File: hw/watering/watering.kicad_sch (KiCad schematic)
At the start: 5 parts, among them J2 USB_C_Receptacle

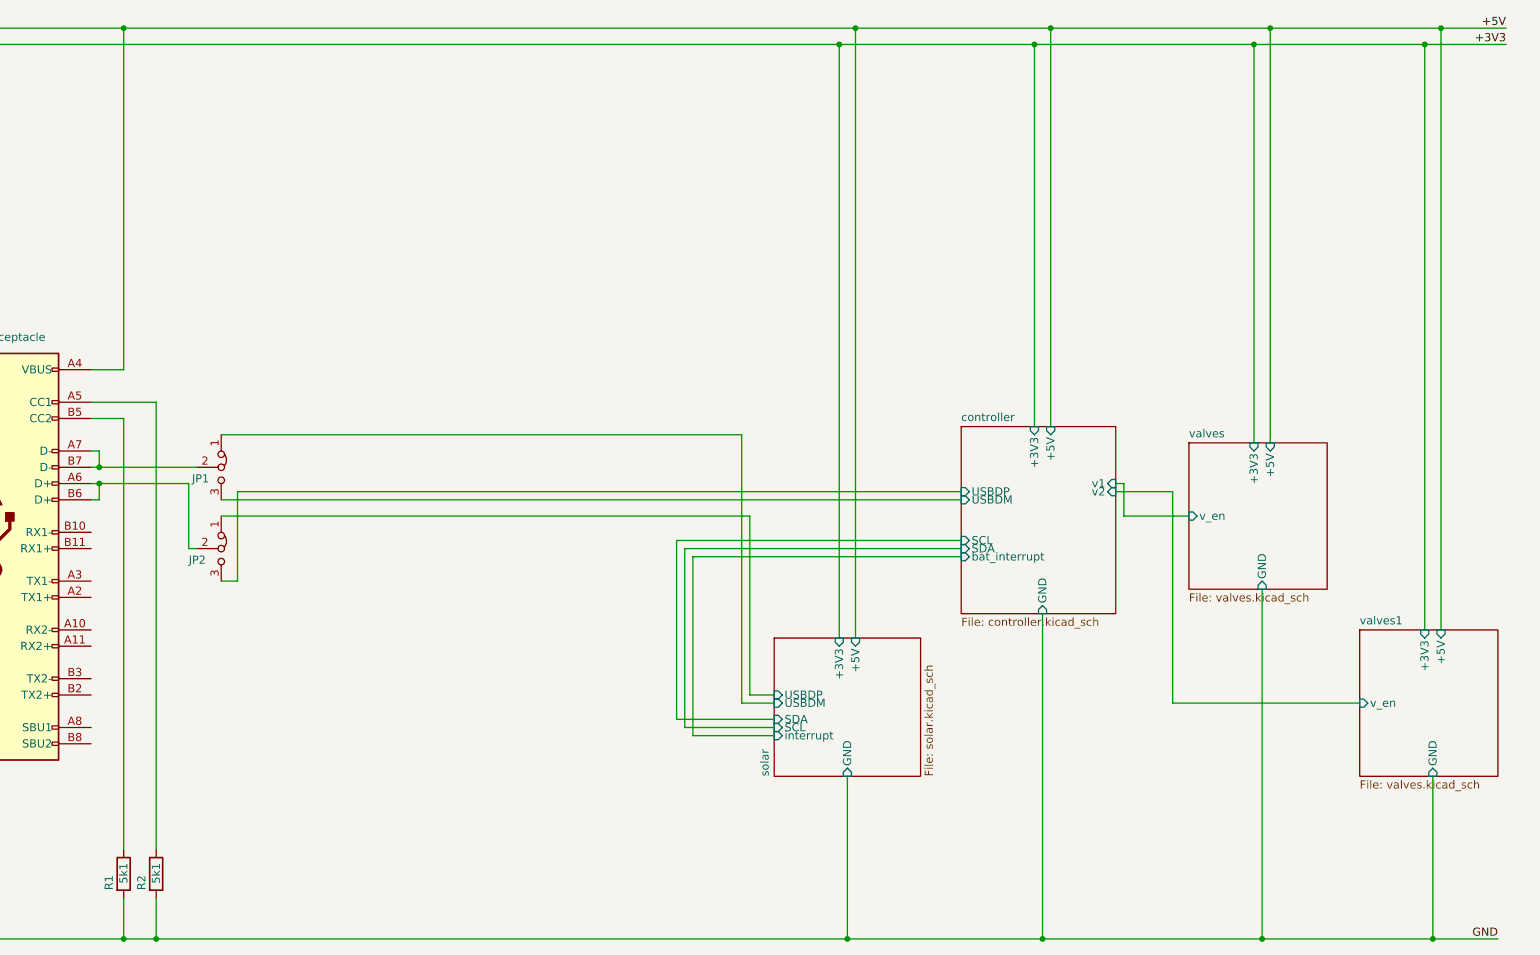
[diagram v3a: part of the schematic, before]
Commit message: added supply chip for battery and solar
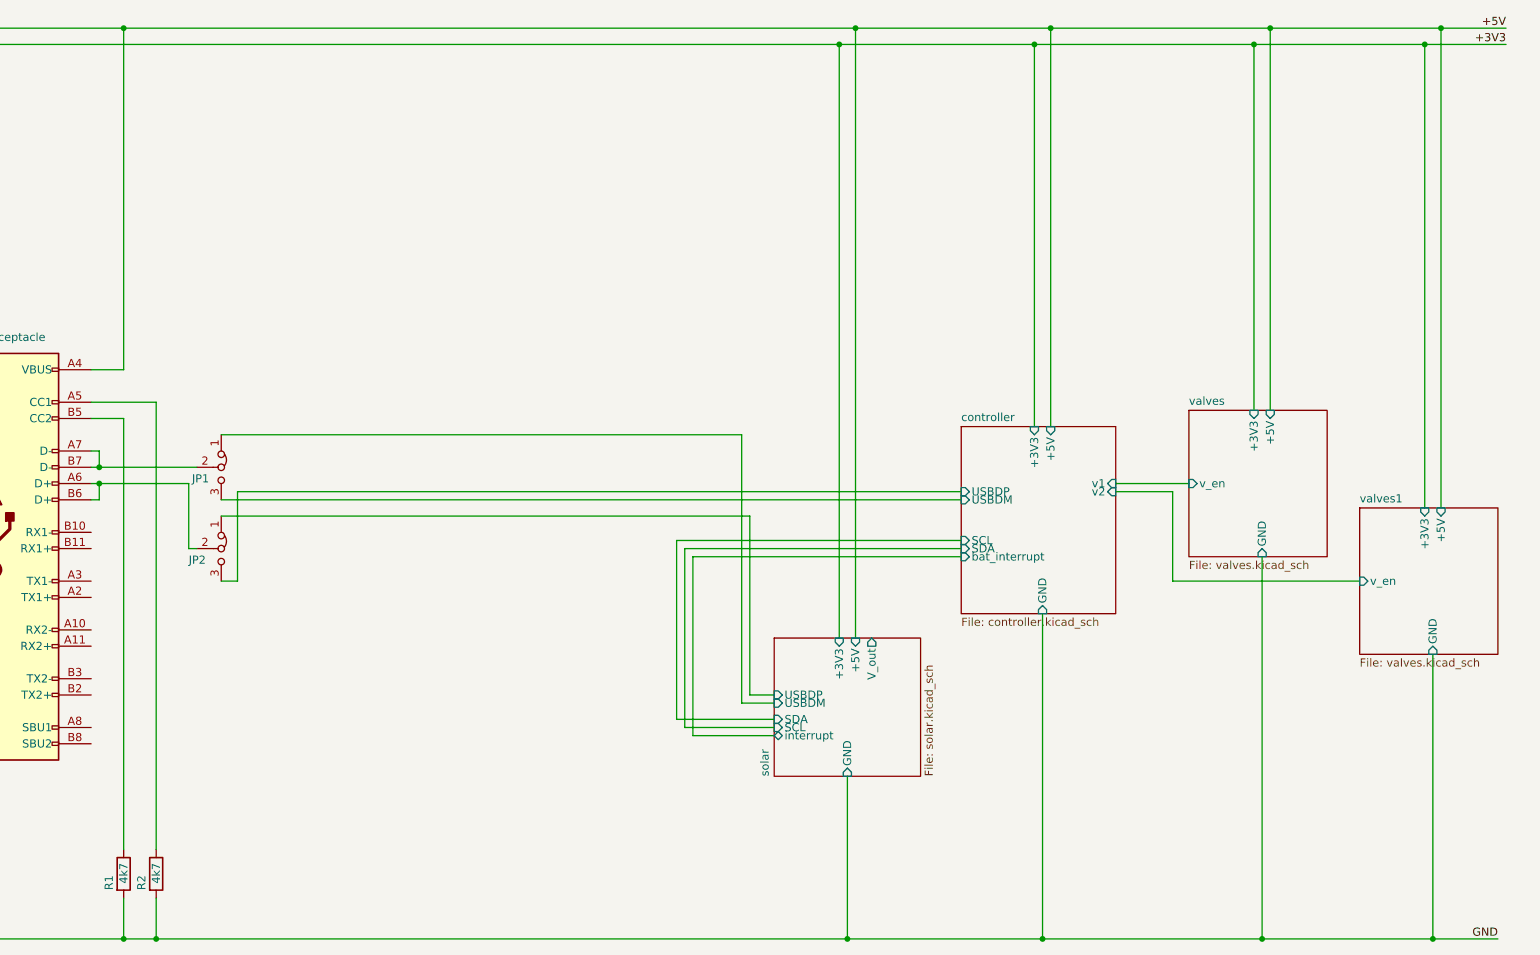
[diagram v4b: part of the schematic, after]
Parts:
- R1, R2: value 5k1 -> 4k7
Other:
- sheet solar ports: added V_out; removed none
- company: (none) -> tomatenkuchen
- title: (none) -> autonomous-watering
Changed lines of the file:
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@@
 	(generator_version "10.0")
 	(paper "A4")
+	(title_block
+		(title "autonomous-watering")
+		(date "2026-05-27")
+		(rev "0")
+		(company "tomatenkuchen")
+		(comment 1 "https://github.com/tomatenkuchen/autonomous-watering")
+	)
+	(junction
+		(at 204.47 161.29)
+		(diameter 0)
+		(color 0 0 0 0)
+	)
+	(junction
+		(at 266.7 19.05)
+		(diameter 0)
+		(color 0 0 0 0)
+	)
+	(junction
+		(at 40.64 161.29)
+		(diameter 0)
+		(color 0 0 0 0)
+	)
+	(junction
+		(at 237.49 21.59)
+		(diameter 0)
+		(color 0 0 0 0)
+	)
+	(junction
+		(at 205.74 19.05)
+		(diameter 0)
+		(color 0 0 0 0)
+	)
 	(junction
 		(at 264.16 21.59)
@@
 	)
 	(junction
-		(at 204.47 161.29)
-		(diameter 0)
-		(color 0 0 0 0)
-	)
-	(junction
-		(at 40.64 161.29)
-		(diameter 0)
-		(color 0 0 0 0)
-	)
-	(junction
-		(at 205.74 19.05)
-		(diameter 0)
-		(color 0 0 0 0)
-	)
-	(junction
-		(at 266.7 19.05)
+		(at 57.15 90.17)
+		(diameter 0)
+		(color 0 0 0 0)
+	)
+	(junction
+		(at 265.43 161.29)
+		(diameter 0)
+		(color 0 0 0 0)
+	)
+	(junction
+		(at 66.04 161.29)
+		(diameter 0)
+		(color 0 0 0 0)
+	)
+	(junction
+		(at 60.96 19.05)
+		(diameter 0)
+		(color 0 0 0 0)
+	)
+	(junction
+		(at 238.76 161.29)
 		(diameter 0)
 		(color 0 0 0 0)
@@
 	)
 	(junction
-		(at 238.76 161.29)
-		(diameter 0)
-		(color 0 0 0 0)
-	)
-	(junction
-		(at 237.49 21.59)
-		(diameter 0)
-		(color 0 0 0 0)
-	)
-	(junction
-		(at 57.15 90.17)
-		(diameter 0)
-		(color 0 0 0 0)
-	)
-	(junction
-		(at 265.43 161.29)
-		(diameter 0)
-		(color 0 0 0 0)
-	)
-	(junction
-		(at 66.04 161.29)
-		(diameter 0)
-		(color 0 0 0 0)
-	)
-	(junction
-		(at 60.96 19.05)
-		(diameter 0)
-		(color 0 0 0 0)
-	)
-	(junction
 		(at 172.72 21.59)
 		(diameter 0)
@@
 	(wire
 		(pts
-			(xy 240.03 83.82) (xy 240.03 19.05)
+			(xy 240.03 78.74) (xy 240.03 19.05)
 		)
 		(stroke
@@
 	(wire
 		(pts
-			(xy 217.17 95.25) (xy 227.33 95.25)
-		)
-		(stroke
-			(width 0)
-			(type default)
-		)
-	)
-	(wire
-		(pts
 			(xy 66.04 161.29) (xy 173.99 161.29)
 		)
@@
 	(wire
 		(pts
-			(xy 224.79 124.46) (xy 254 124.46)
+			(xy 224.79 105.41) (xy 254 105.41)
 		)
 		(stroke
@@
 	(wire
 		(pts
-			(xy 266.7 113.03) (xy 266.7 19.05)
+			(xy 266.7 93.98) (xy 266.7 19.05)
 		)
 		(stroke
@@
 	(wire
 		(pts
-			(xy 265.43 135.89) (xy 265.43 161.29)
+			(xy 265.43 116.84) (xy 265.43 161.29)
 		)
 		(stroke
@@
 	(wire
 		(pts
-			(xy 237.49 83.82) (xy 237.49 21.59)
+			(xy 237.49 78.74) (xy 237.49 21.59)
 		)
 		(stroke
@@
 	(wire
 		(pts
-			(xy 238.76 106.68) (xy 238.76 161.29)
+			(xy 238.76 101.6) (xy 238.76 161.29)
 		)
 		(stroke
@@
 	(wire
 		(pts
-			(xy 217.17 90.17) (xy 217.17 95.25)
-		)
-		(stroke
-			(width 0)
-			(type default)
-		)
-	)
-	(wire
-		(pts
 			(xy 203.2 81.28) (xy 203.2 21.59)
 		)
@@
 	(wire
 		(pts
-			(xy 264.16 113.03) (xy 264.16 21.59)
+			(xy 264.16 93.98) (xy 264.16 21.59)
 		)
 		(stroke
@@
 	(wire
 		(pts
-			(xy 224.79 91.44) (xy 224.79 124.46)
+			(xy 224.79 91.44) (xy 224.79 105.41)
 		)
 		(stroke
@@
 	(wire
 		(pts
-			(xy 215.9 90.17) (xy 217.17 90.17)
+			(xy 215.9 90.17) (xy 227.33 90.17)
 		)
 		(stroke
@@
 			)
 		)
-		(property "Value" "5k1"
+		(property "Value" "4k7"
 			(at 66.04 152.654 90)
 			(show_name no)
@@
 			)
 		)
-		(property "Value" "5k1"
+		(property "Value" "4k7"
 			(at 60.96 152.654 90)
 			(show_name no)
@@
 	)
 	(sheet
-		(at 254 113.03)
+		(at 254 93.98)
 		(size 21.59 22.86)
 		(exclude_from_sim no)
@@
 		)
 		(property "Sheetname" "valves1"
-			(at 254 112.3184 0)
+			(at 254 93.2684 0)
 			(show_name no)
 			(do_not_autoplace no)
@@
 		)
 		(property "Sheetfile" "valves.kicad_sch"
-			(at 254 136.4746 0)
+			(at 254 117.4246 0)
 			(show_name no)
 			(do_not_autoplace no)
@@
 		)
 		(pin "+3V3" input
-			(at 264.16 113.03 90)
+			(at 264.16 93.98 90)
 			(effects
 				(font
@@
 		)
 		(pin "+5V" input
-			(at 266.7 113.03 90)
+			(at 266.7 93.98 90)
 			(effects
 				(font
@@
 		)
 		(pin "GND" input
-			(at 265.43 135.89 270)
+			(at 265.43 116.84 270)
 			(effects
 				(font
@@
 		)
 		(pin "v_en" input
-			(at 254 124.46 180)
+			(at 254 105.41 180)
 			(effects
 				(font
@@
 	)
 	(sheet
-		(at 227.33 83.82)
+		(at 227.33 78.74)
 		(size 21.59 22.86)
 		(exclude_from_sim no)
@@
 		)
 		(property "Sheetname" "valves"
-			(at 227.33 83.1084 0)
+			(at 227.33 78.0284 0)
 			(show_name no)
 			(do_not_autoplace no)
@@
 		)
 		(property "Sheetfile" "valves.kicad_sch"
-			(at 227.33 107.2646 0)
+			(at 227.33 102.1846 0)
 			(show_name no)
 			(do_not_autoplace no)
@@
 		)
 		(pin "+3V3" input
-			(at 237.49 83.82 90)
+			(at 237.49 78.74 90)
 			(effects
 				(font
@@
 		)
 		(pin "+5V" input
-			(at 240.03 83.82 90)
+			(at 240.03 78.74 90)
 			(effects
 				(font
@@
 		)
 		(pin "GND" input
-			(at 238.76 106.68 270)
+			(at 238.76 101.6 270)
 			(effects
 				(font
@@
 		)
 		(pin "v_en" input
-			(at 227.33 95.25 180)
+			(at 227.33 90.17 180)
 			(effects
 				(font
@@
 			)
 		)
-		(pin "interrupt" input
+		(pin "interrupt" tri_state
 			(at 162.56 129.54 180)
 			(effects
@@
 			)
 		)
+		(pin "V_out" output
+			(at 177.8 114.3 90)
+			(effects
+				(font
+					(size 1.27 1.27)
+				)
+				(justify right)
+			)
+		)

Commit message: updated power
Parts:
- removed JP1, JP2: Jumper_3_Bridged12, Connector_PinHeader_2.54mm:PinHeader_1x03_P2.54mm_Vertical, symbol Jumper:Jumper_3_Bridged12
- J2: footprint (none) -> Connector_USB:USB_C_Receptacle_GCT_USB4105-xx-A_16P_TopMnt_Horizontal
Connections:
- net controller/USBDM: now also J2.A7 (D-), J2.B7 (D-)
- net controller/USBDP: now also J2.A6 (D+), J2.B6 (D+)
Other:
- removed sheet valves
- added sheet valves2 (valves.kicad_sch)
- sheet controller ports: added none; removed +5V, SCL, SDA, bat_interrupt
- sheet solar ports: added solar_enable, solar_pwm, v_en; removed SCL, SDA, USBDM, USBDP, V_out, interrupt
- sheet valves1 ports: added none; removed +5V

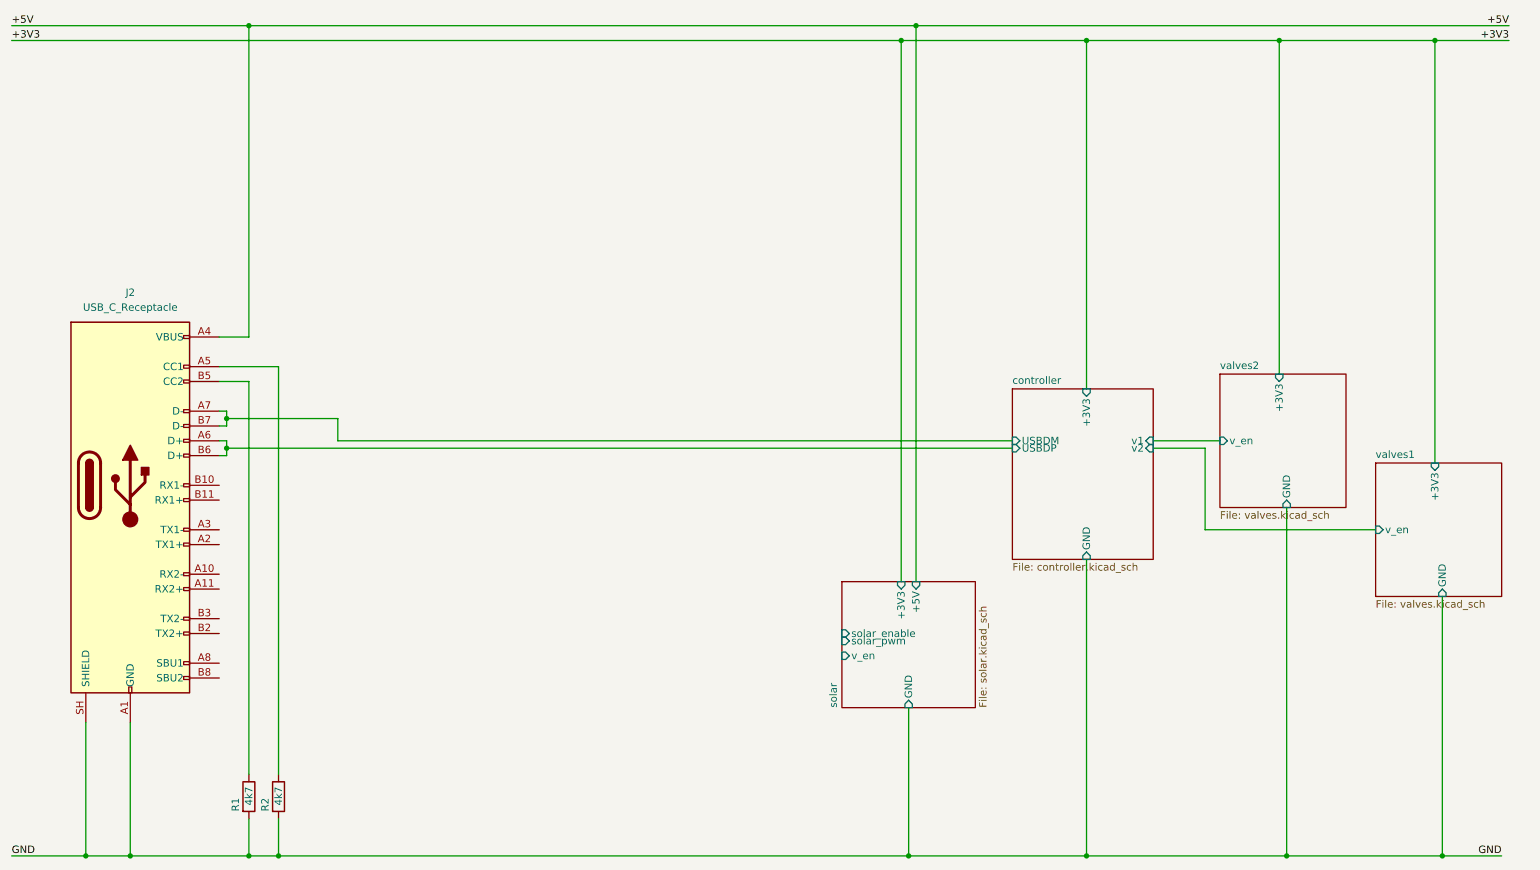
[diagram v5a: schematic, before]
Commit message: connections completet. started placing and routing
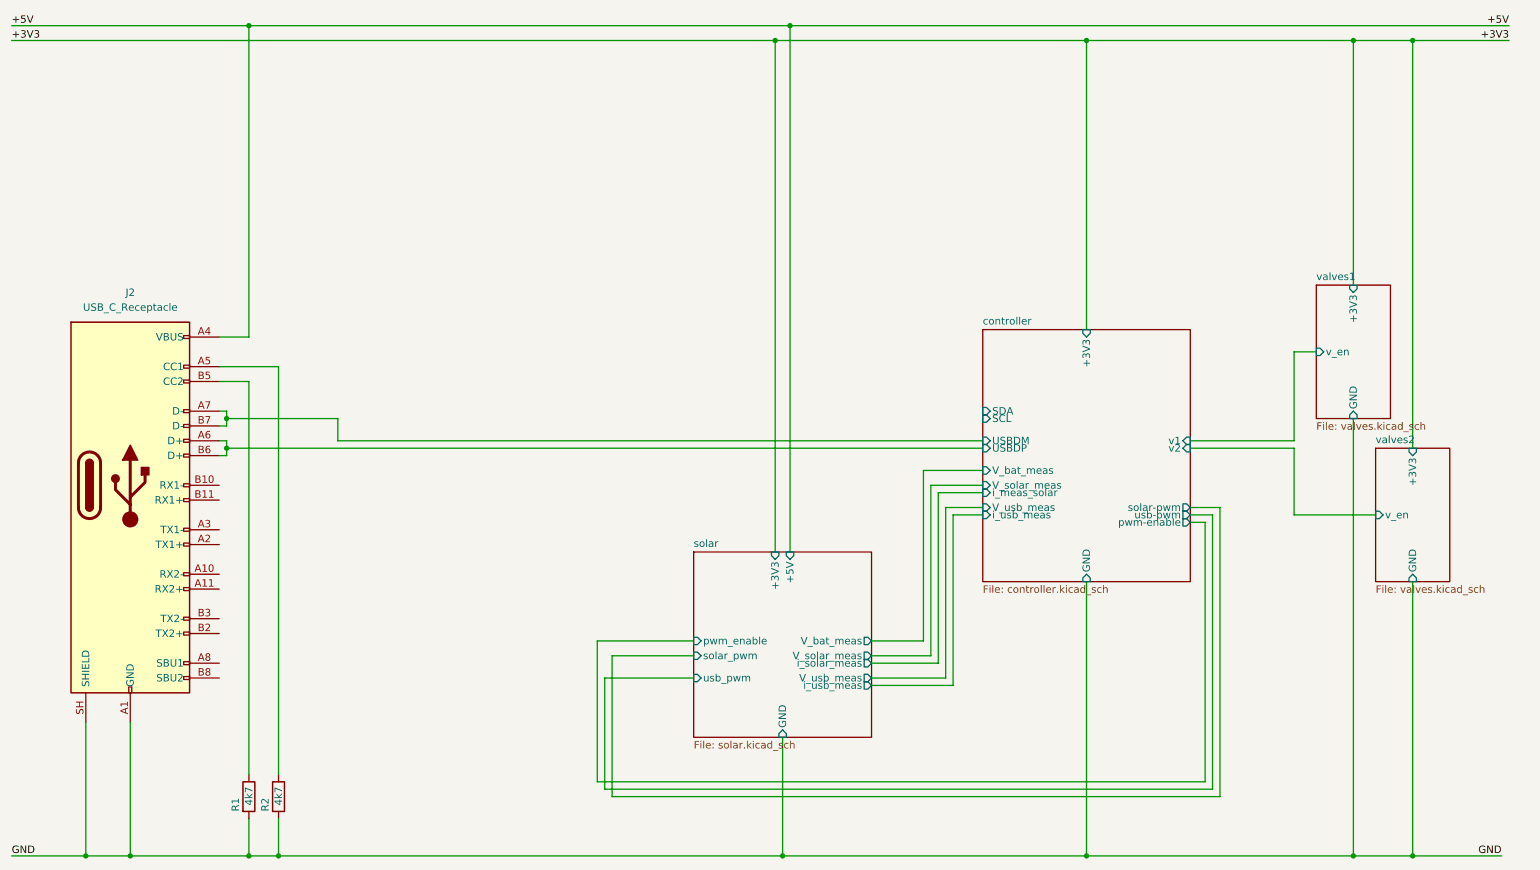
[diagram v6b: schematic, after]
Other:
- sheet controller ports: added SCL, SDA, V_bat_meas, V_solar_meas, V_usb_meas, i_meas_solar, i_usb_meas, pwm-enable, solar-pwm, usb-pwm; removed none
- sheet solar ports: added V_bat_meas, V_solar_meas, V_usb_meas, i_solar_meas, i_usb_meas, pwm_enable, usb_pwm; removed solar_enable, v_en

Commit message: some more placing
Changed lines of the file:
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@@
 	(wire
 		(pts
-			(xy 121.92 149.86) (xy 121.92 130.81)
+			(xy 121.92 149.86) (xy 121.92 129.54)
 		)
 		(stroke
@@
 	(wire
 		(pts
-			(xy 121.92 130.81) (xy 137.16 130.81)
+			(xy 121.92 129.54) (xy 137.16 129.54)
 		)
 		(stroke
@@
 		)
 		(pin "usb_pwm" input
-			(at 137.16 130.81 180)
-			(effects
-				(font
+			(at 137.16 129.54 180)
+			(effects
+				(font

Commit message: routing done
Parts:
- added C19: 1u, Capacitor_SMD:C_0603_1608Metric, symbol Device:C
- added D1, D2: SMBJ6.5CA, Diode_SMD:D_SMB, symbol Diode:1N62xxCA
- added R29: 47k, Resistor_SMD:R_0603_1608Metric, symbol Device:R
- added R30: 10k, Resistor_SMD:R_0603_1608Metric, symbol Device:R
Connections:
- net +5V: now also R29.2
- net GND: now also C19.2, D1.1 (A1), D2.1 (A1), R30.2
- net controller/USBDM: now also D2.2 (A2)
- net controller/USBDP: now also D1.2 (A2)
- new net V_usb_avail: C19.1, R29.1, R30.1
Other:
- added sheet conductivity (conductivity.kicad_sch)
- sheet controller ports: added V_usb_avail, cond_en, cond_pwm, i_cond_meas; removed V_usb_meas
- sheet solar ports: added none; removed V_usb_meas
- moved on the sheet: J2, R1, R2
